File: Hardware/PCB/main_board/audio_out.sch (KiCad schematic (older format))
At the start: 2 parts, among them J5 Conn_Coaxial, J6 AudioJack2

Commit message: Flip connectors, add 3D models
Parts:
- removed J6: AudioJack2, symbol Connector:AudioJack2
- added J6: AudioJack3, lib:audio_jack_3.5mm_KYCON_STX-3000, symbol Connector:AudioJack3
- J5: footprint (none) -> lib:rca_black
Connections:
- wire segments 3 -> 4
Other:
- note added: "mono -> ring unused"
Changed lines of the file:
@@
 F 0 "J5" H 7650 1775 50  0000 L CNN
 F 1 "Conn_Coaxial" H 7650 1684 50  0000 L CNN
-F 2 "" H 7550 1800 50  0001 C CNN
+F 2 "lib:rca_black" H 7550 1800 50  0001 C CNN
 F 3 " ~" H 7550 1800 50  0001 C CNN
 	1    7550 1800
@@
 Wire Wire Line
 	7550 2050 7550 2000
-$Comp
-L Connector:AudioJack2 J6
-U 1 1 5E685921
-P 7550 3100
-F 0 "J6" H 7370 3083 50  0000 R CNN
-F 1 "AudioJack2" H 7370 3174 50  0000 R CNN
-F 2 "" H 7550 3100 50  0001 C CNN
-F 3 "~" H 7550 3100 50  0001 C CNN
-	1    7550 3100
-	-1   0    0    1
-$EndComp
 $Comp
 L power:GND #PWR018
@@
 Text Notes 7750 3450 0    118  ~ 24
 Audio headphones level
+$Comp
+L Connector:AudioJack3 J6
+U 1 1 5E55D40F
+P 7550 3100
+F 0 "J6" H 7270 3033 50  0000 R CNN
+F 1 "AudioJack3" H 7270 3124 50  0000 R CNN
+F 2 "lib:audio_jack_3.5mm_KYCON_STX-3000" H 7550 3100 50  0001 C CNN
+F 3 "~" H 7550 3100 50  0001 C CNN
+	1    7550 3100
+	-1   0    0    1
+$EndComp
+Wire Wire Line
+	7350 3000 6950 3000
+Text Notes 7350 3100 2    50   ~ 0
+mono -> ring unused
 $EndSCHEMATC

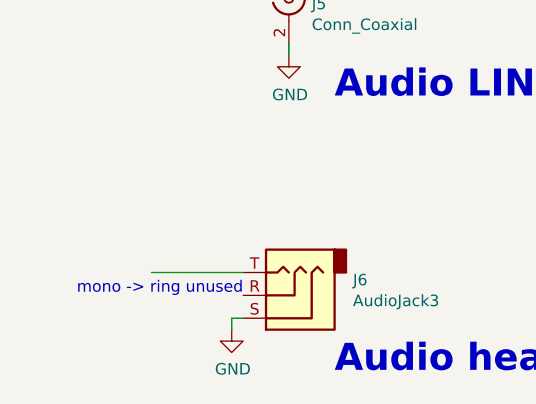
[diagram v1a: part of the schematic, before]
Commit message: Route GPIO
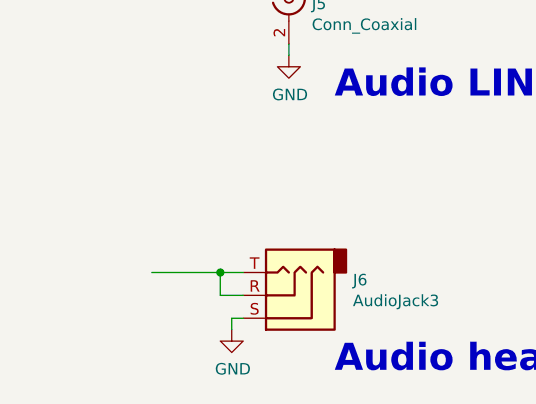
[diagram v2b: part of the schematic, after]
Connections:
- wire segments 4 -> 7
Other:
- note removed: "mono -> ring unused"
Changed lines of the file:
@@
 $Descr A4 11693 8268
 encoding utf-8
-Sheet 5 7
+Sheet 4 7
 Title ""
 Date ""
@@
 $EndComp
 Wire Wire Line
-	7350 3000 6950 3000
-Text Notes 7350 3100 2    50   ~ 0
-mono -> ring unused
+	7350 3000 7250 3000
+Wire Wire Line
+	7350 3100 7250 3100
+Wire Wire Line
+	7250 3100 7250 3000
+Connection ~ 7250 3000
+Wire Wire Line
+	7250 3000 6950 3000
 $EndSCHEMATC

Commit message: Route PWR
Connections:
- no-connect marks 0 -> 2
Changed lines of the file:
@@
 Wire Wire Line
 	7250 3000 6950 3000
+NoConn ~ 7350 1800
+NoConn ~ 6950 3000
 $EndSCHEMATC

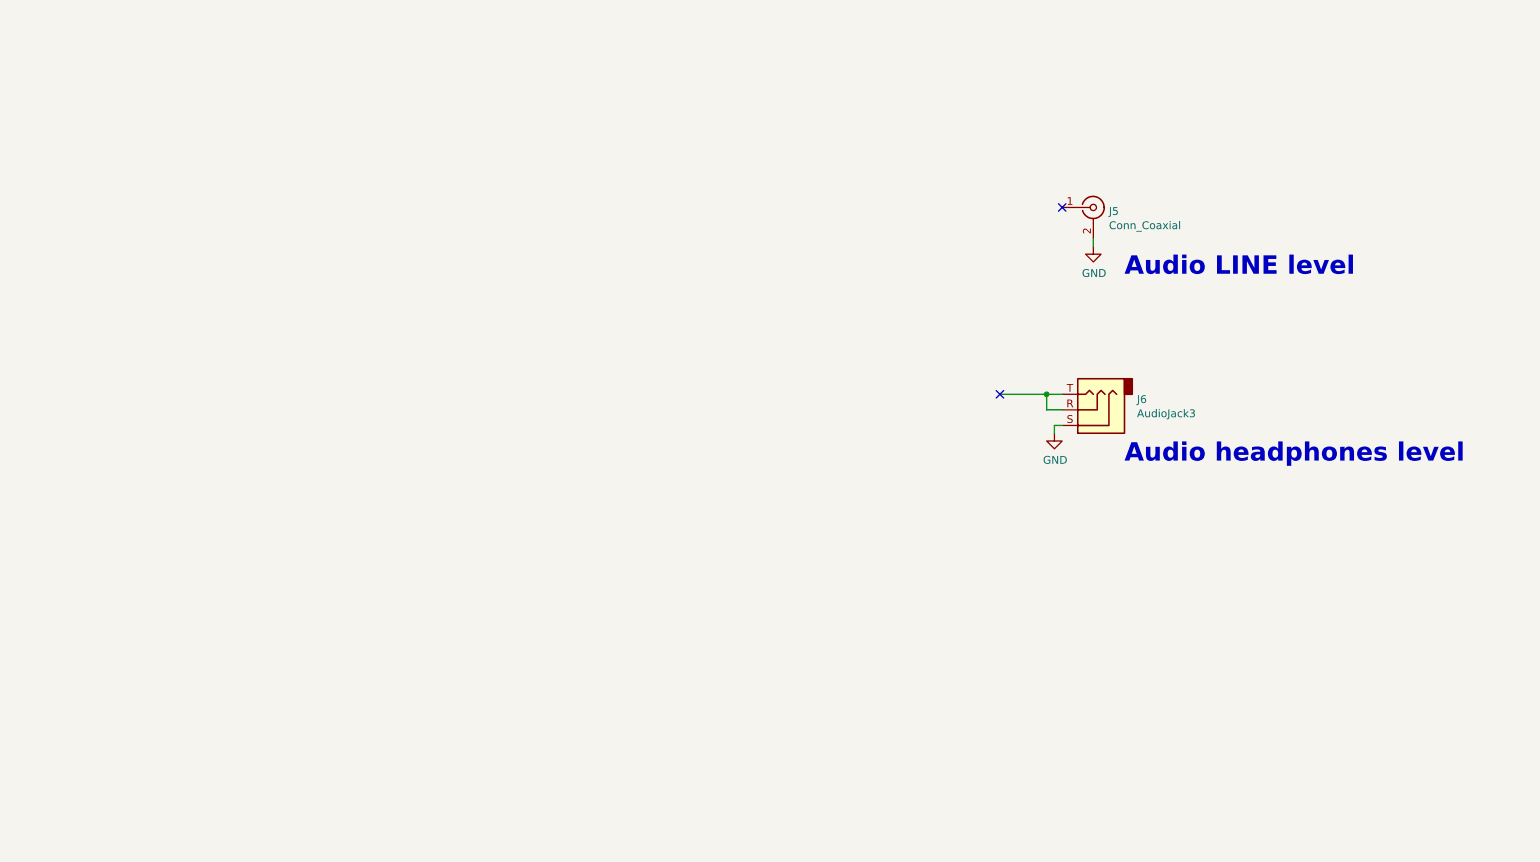
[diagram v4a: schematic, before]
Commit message: Add FX buffer and headphone amp to schematics
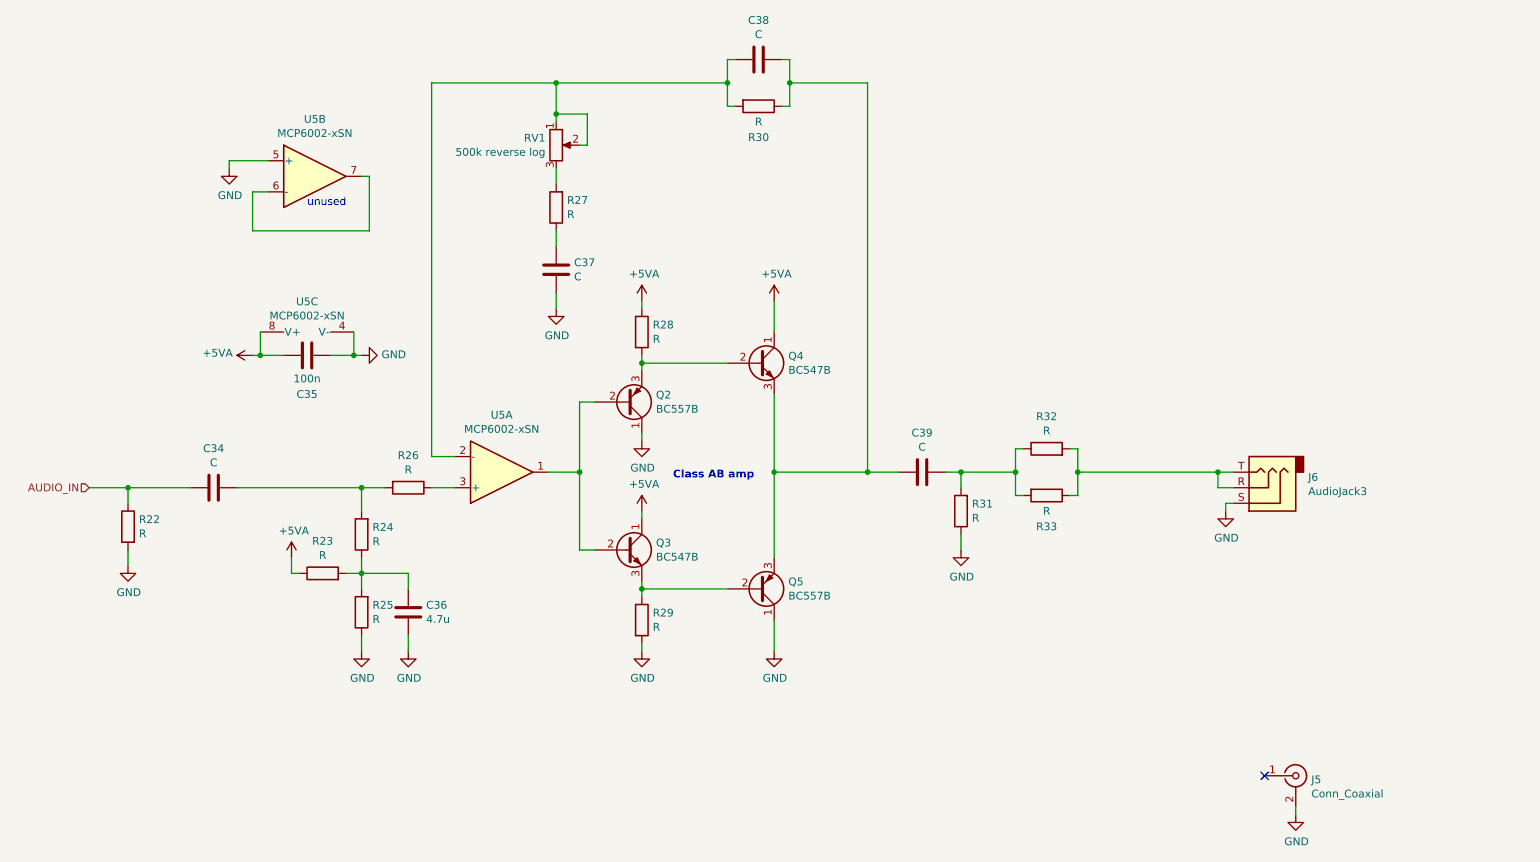
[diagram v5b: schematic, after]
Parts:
- added C34, C37, C38, C39: C, symbol Device:C
- added C35: 100n, symbol Device:C
- added C36: 4.7u, symbol Device:C
- added Q2, Q5: BC557B, Package_TO_SOT_THT:TO-92_Inline, symbol Transistor_BJT:BC557
- added Q3, Q4: BC547B, Package_TO_SOT_THT:TO-92_Inline, symbol Transistor_BJT:BC547
- added R22, R23, R24, R25, R26, R27, R28, R29, R30, R31, R32, R33: R, symbol Device:R
- added RV1: 500k reverse log, symbol Device:R_POT
- added U5: MCP6002-xSN, symbol Amplifier_Operational:MCP6002-xSN
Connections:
- net GND: now also C35.1, C36.1, C37.1, Q2.1 (C), Q5.1 (C), R22.2, R25.1, R29.2, R31.1, U5.4 (V-), U5.5 (+)
- net at J6.R, J6.T: now also R32.2, R33.1
- new net: R26.1, U5.3 (+)
- new net: C34.1, R24.2, R26.2
- new net: Q2.2 (B), Q3.2 (B), U5.1
- new net: C38.2, R30.2, RV1.1, RV1.2, U5.2 (-)
- new net: U5.6 (-), U5.7
- new net: R27.2, RV1.3
- new net: Q2.3 (E), Q4.2 (B), R28.2
- new net: C38.1, C39.2, Q4.3 (E), Q5.3 (E), R30.1
- new net: Q3.3 (E), Q5.2 (B), R29.1
- new net: C36.2, R23.2, R24.1, R25.2
- new net: C39.1, R31.2, R32.1, R33.2
- new net: C37.2, R27.1
- new net +5VA: C35.2, Q3.1 (C), Q4.1 (C), R23.1, R28.1, U5.8 (V+)
- new net AUDIO_IN: C34.2, R22.1
- no-connect marks 2 -> 1
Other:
- note added: "Class AB amp"
- note added: "unused"
- note removed: "Audio LINE level"
- note removed: "Audio headphones level"
- moved on the sheet: J5, J6

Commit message: Route PCB changes
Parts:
- removed C36: 4.7u, symbol Device:C
- removed C39: C, symbol Device:C
- removed Q2, Q5: BC557B, Package_TO_SOT_THT:TO-92_Inline, symbol Transistor_BJT:BC557
- removed Q3, Q4: BC547B, Package_TO_SOT_THT:TO-92_Inline, symbol Transistor_BJT:BC547
- added C36, C39: 47u, Capacitor_SMD:CP_Elec_6.3x5.4, symbol Device:CP
- added Q1, Q4: BC857B, Package_TO_SOT_SMD:SOT-23, symbol Transistor_BJT:BC857
- added Q2, Q3: BC847B, Package_TO_SOT_SMD:SOT-23, symbol Transistor_BJT:BC847
- C34: value C -> 100n; footprint (none) -> Capacitor_SMD:C_0805_2012Metric
- C35: footprint (none) -> Capacitor_SMD:C_0805_2012Metric
- C37: value C -> 4.7u; footprint (none) -> Capacitor_SMD:C_0805_2012Metric
- C38: value C -> 150p; footprint (none) -> Capacitor_SMD:C_0805_2012Metric
- R22: value R -> 22M; footprint (none) -> Resistor_SMD:R_0805_2012Metric
- R23, R25, R28, R29, R31: value R -> 10k; footprint (none) -> Resistor_SMD:R_0805_2012Metric
- R24: value R -> 10M; footprint (none) -> Resistor_SMD:R_0805_2012Metric
- R26: value R -> 1k; footprint (none) -> Resistor_SMD:R_0805_2012Metric
- R27: value R -> 33; footprint (none) -> Resistor_SMD:R_0805_2012Metric
- R30: value R -> 56k; footprint (none) -> Resistor_SMD:R_0805_2012Metric
- R32, R33: value R -> 100; footprint (none) -> Resistor_SMD:R_0805_2012Metric
- RV_VOL1: renamed from RV1; footprint (none) -> Potentiometer_THT:Potentiometer_Alps_RK09K_Single_Vertical
- U5: footprint (none) -> Package_SO:SOIC-8_3.9x4.9mm_P1.27mm
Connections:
- net +5VA: now also Q2.3 (C), Q3.3 (C)
- net GND: now also C36.2, Q1.3 (C), Q4.3 (C)
- net at U5.1: now also Q1.1 (B), Q2.1 (B)
- net at R28.2: now also Q1.2 (E), Q3.1 (B)
- net at C38.1, R30.1: now also C39.1, Q3.2 (E), Q4.2 (E)
- net at R29.1: now also Q2.2 (E), Q4.1 (B)
- net at R23.2, R24.1, R25.2: now also C36.1
- net at R31.2, R32.1, R33.2: now also C39.2

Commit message: Add test points headers
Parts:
- added J12: Audio_post_AB_amp, Connector_PinHeader_2.54mm:PinHeader_1x01_P2.54mm_Vertical, symbol Connector_Generic:Conn_01x01
- added J13: Audio_out_jack, Connector_PinHeader_2.54mm:PinHeader_1x01_P2.54mm_Vertical, symbol Connector_Generic:Conn_01x01
- added J14: Audio_out_RCA, Connector_PinHeader_2.54mm:PinHeader_1x01_P2.54mm_Vertical, symbol Connector_Generic:Conn_01x01
- added J9: Audio_pre_AB_amp, Connector_PinHeader_2.54mm:PinHeader_1x01_P2.54mm_Vertical, symbol Connector_Generic:Conn_01x01
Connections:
- net Audio_out_jack: now reaches J6.R, J6.T, R32.2, R33.1
- net Audio_out_jack: now also J13.1 (Pin_1)
- net Audio_out_RCA: now reaches J5.1 (In)
- net Audio_out_RCA: now also J14.1 (Pin_1)
- net audio_pre_AB_amp: now reaches Q1.1 (B), Q2.1 (B), U5.1
- net audio_pre_AB_amp: now also J9.1 (Pin_1)
- net audio_post_AB_amp: now reaches C38.1, C39.1, Q3.2 (E), Q4.2 (E), R30.1
- net audio_post_AB_amp: now also J12.1 (Pin_1)
- no-connect marks 1 -> 0
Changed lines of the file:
@@
 Wire Wire Line
 	7450 3500 7450 3650
-NoConn ~ 8650 5450
 Wire Wire Line
 	7450 3500 8350 3500
@@
 	1    0    0    1
 $EndComp
+Wire Wire Line
+	9200 1200 9100 1200
+Wire Wire Line
+	9100 1500 9200 1500
+Wire Wire Line
+	9100 1800 9200 1800
+Text Label 7650 3500 0    50   ~ 0
+Audio_out_jack
+Text Label 9100 1800 2    50   ~ 0
+Audio_out_jack
+Text Label 5550 3500 0    50   ~ 0
+audio_post_AB_amp
+Text Label 4250 3800 1    50   ~ 0
+audio_pre_AB_amp
+Text Label 9100 1500 2    50   ~ 0
+audio_post_AB_amp
+Text Label 9100 1200 2    50   ~ 0
+audio_pre_AB_amp
+Wire Wire Line
+	9100 2100 9200 2100
+Text Label 9100 2100 2    50   ~ 0
+Audio_out_RCA
+Text Label 8550 5450 2    50   ~ 0
+Audio_out_RCA
+Wire Wire Line
+	8550 5450 8650 5450
+$Comp
+L Connector_Generic:Conn_01x01 J?
+U 1 1 5E8E9A39
+P 9400 1200
+AR Path="/5E57C92D/5E8E9A39" Ref="J?"  Part="1"
+AR Path="/5E68385C/5E8E9A39" Ref="J9"  Part="1"
+F 0 "J9" H 9480 1242 50  0000 L CNN
+F 1 "Audio_pre_AB_amp" H 9480 1151 50  0000 L CNN
+F 2 "Connector_PinHeader_2.54mm:PinHeader_1x01_P2.54mm_Vertical" H 9400 1200 50  0001 C CNN
+F 3 "~" H 9400 1200 50  0001 C CNN
+	1    9400 1200
+	1    0    0    -1
+$EndComp
+$Comp
+L Connector_Generic:Conn_01x01 J?
+U 1 1 5E8EC39B
+P 9400 1500
+AR Path="/5E57C92D/5E8EC39B" Ref="J?"  Part="1"
+AR Path="/5E68385C/5E8EC39B" Ref="J12"  Part="1"
+F 0 "J12" H 9480 1542 50  0000 L CNN
+F 1 "Audio_post_AB_amp" H 9480 1451 50  0000 L CNN
+F 2 "Connector_PinHeader_2.54mm:PinHeader_1x01_P2.54mm_Vertical" H 9400 1500 50  0001 C CNN
+F 3 "~" H 9400 1500 50  0001 C CNN
+	1    9400 1500
+	1    0    0    -1
+$EndComp
+$Comp
+L Connector_Generic:Conn_01x01 J?
+U 1 1 5E8ECAF9
+P 9400 1800
+AR Path="/5E57C92D/5E8ECAF9" Ref="J?"  Part="1"
+AR Path="/5E68385C/5E8ECAF9" Ref="J13"  Part="1"
+F 0 "J13" H 9480 1842 50  0000 L CNN
+F 1 "Audio_out_jack" H 9480 1751 50  0000 L CNN
+F 2 "Connector_PinHeader_2.54mm:PinHeader_1x01_P2.54mm_Vertical" H 9400 1800 50  0001 C CNN
+F 3 "~" H 9400 1800 50  0001 C CNN
+	1    9400 1800
+	1    0    0    -1
+$EndComp
+$Comp
+L Connector_Generic:Conn_01x01 J?
+U 1 1 5E8EF8B9
+P 9400 2100
+AR Path="/5E57C92D/5E8EF8B9" Ref="J?"  Part="1"
+AR Path="/5E68385C/5E8EF8B9" Ref="J14"  Part="1"
+F 0 "J14" H 9480 2142 50  0000 L CNN
+F 1 "Audio_out_RCA" H 9480 2051 50  0000 L CNN
+F 2 "Connector_PinHeader_2.54mm:PinHeader_1x01_P2.54mm_Vertical" H 9400 2100 50  0001 C CNN
+F 3 "~" H 9400 2100 50  0001 C CNN
+	1    9400 2100
+	1    0    0    -1
+$EndComp
 $EndSCHEMATC

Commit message: Re-layout HMI, pre route
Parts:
- removed J14: Audio_out_RCA, Connector_PinHeader_2.54mm:PinHeader_1x01_P2.54mm_Vertical, symbol Connector_Generic:Conn_01x01
- removed J5: Conn_Coaxial, lib:rca_black, symbol Connector:Conn_Coaxial
- J12: value Audio_post_AB_amp -> Post_AB_amp; footprint Connector_PinHeader_2.54mm:PinHeader_1x01_P2.54mm_Vertical -> TestPoint:TestPoint_THTPad_D1.0mm_Drill0.5mm; symbol Connector_Generic:Conn_01x01 -> Connector:TestPoint
- J13: footprint Connector_PinHeader_2.54mm:PinHeader_1x01_P2.54mm_Vertical -> TestPoint:TestPoint_THTPad_D1.0mm_Drill0.5mm; symbol Connector_Generic:Conn_01x01 -> Connector:TestPoint
- J9: value Audio_pre_AB_amp -> Pre_AB_amp; footprint Connector_PinHeader_2.54mm:PinHeader_1x01_P2.54mm_Vertical -> TestPoint:TestPoint_THTPad_D1.0mm_Drill0.5mm; symbol Connector_Generic:Conn_01x01 -> Connector:TestPoint
- RV_VOL1: footprint Potentiometer_THT:Potentiometer_Alps_RK09K_Single_Vertical -> Potentiometer_THT:Potentiometer_Alps_RK09K_Single_Horizontal
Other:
- note added: "Test points"
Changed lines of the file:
@@
 $EndDescr
-$Comp
-L Connector:Conn_Coaxial J5
-U 1 1 5E6845CE
-P 8850 5450
-F 0 "J5" H 8950 5425 50  0000 L CNN
-F 1 "Conn_Coaxial" H 8950 5334 50  0000 L CNN
-F 2 "lib:rca_black" H 8850 5450 50  0001 C CNN
-F 3 " ~" H 8850 5450 50  0001 C CNN
-	1    8850 5450
-	1    0    0    -1
-$EndComp
-$Comp
-L power:GND #PWR019
-U 1 1 5E684B9C
-P 8850 5700
-F 0 "#PWR019" H 8850 5450 50  0001 C CNN
-F 1 "GND" H 8855 5527 50  0000 C CNN
-F 2 "" H 8850 5700 50  0001 C CNN
-F 3 "" H 8850 5700 50  0001 C CNN
-	1    8850 5700
-	1    0    0    -1
-$EndComp
-Wire Wire Line
-	8850 5700 8850 5650
 $Comp
 L power:GND #PWR018
@@
 F 0 "RV_VOL1" H 4031 1446 50  0000 R CNN
 F 1 "500k reverse log" H 4031 1355 50  0000 R CNN
-F 2 "Potentiometer_THT:Potentiometer_Alps_RK09K_Single_Vertical" H 4100 1400 50  0001 C CNN
+F 2 "Potentiometer_THT:Potentiometer_Alps_RK09K_Single_Horizontal" H 4100 1400 50  0001 C CNN
 F 3 "~" H 4100 1400 50  0001 C CNN
 	1    4100 1400
@@
 Text Label 9100 1200 2    50   ~ 0
 audio_pre_AB_amp
-Wire Wire Line
-	9100 2100 9200 2100
-Text Label 9100 2100 2    50   ~ 0
-Audio_out_RCA
-Text Label 8550 5450 2    50   ~ 0
-Audio_out_RCA
-Wire Wire Line
-	8550 5450 8650 5450
-$Comp
-L Connector_Generic:Conn_01x01 J?
+$Comp
+L Connector:TestPoint J?
 U 1 1 5E8E9A39
-P 9400 1200
+P 9200 1200
 AR Path="/5E57C92D/5E8E9A39" Ref="J?"  Part="1"
 AR Path="/5E68385C/5E8E9A39" Ref="J9"  Part="1"
-F 0 "J9" H 9480 1242 50  0000 L CNN
-F 1 "Audio_pre_AB_amp" H 9480 1151 50  0000 L CNN
-F 2 "Connector_PinHeader_2.54mm:PinHeader_1x01_P2.54mm_Vertical" H 9400 1200 50  0001 C CNN
-F 3 "~" H 9400 1200 50  0001 C CNN
-	1    9400 1200
-	1    0    0    -1
-$EndComp
-$Comp
-L Connector_Generic:Conn_01x01 J?
+F 0 "J9" V 9280 1242 50  0000 L CNN
+F 1 "Pre_AB_amp" V 9200 1400 50  0000 L CNN
+F 2 "TestPoint:TestPoint_THTPad_D1.0mm_Drill0.5mm" H 9200 1200 50  0001 C CNN
+F 3 "~" H 9200 1200 50  0001 C CNN
+	1    9200 1200
+	0    1    1    0
+$EndComp
+$Comp
+L Connector:TestPoint J?
 U 1 1 5E8EC39B
-P 9400 1500
+P 9200 1500
 AR Path="/5E57C92D/5E8EC39B" Ref="J?"  Part="1"
 AR Path="/5E68385C/5E8EC39B" Ref="J12"  Part="1"
-F 0 "J12" H 9480 1542 50  0000 L CNN
-F 1 "Audio_post_AB_amp" H 9480 1451 50  0000 L CNN
-F 2 "Connector_PinHeader_2.54mm:PinHeader_1x01_P2.54mm_Vertical" H 9400 1500 50  0001 C CNN
-F 3 "~" H 9400 1500 50  0001 C CNN
-	1    9400 1500
-	1    0    0    -1
-$EndComp
-$Comp
-L Connector_Generic:Conn_01x01 J?
+F 0 "J12" V 9280 1542 50  0000 L CNN
+F 1 "Post_AB_amp" V 9200 1700 50  0000 L CNN
+F 2 "TestPoint:TestPoint_THTPad_D1.0mm_Drill0.5mm" H 9200 1500 50  0001 C CNN
+F 3 "~" H 9200 1500 50  0001 C CNN
+	1    9200 1500
+	0    1    1    0
+$EndComp
+Text Notes 9000 2100 0    118  ~ 0
+Test points
+$Comp
+L Connector:TestPoint J?
 U 1 1 5E8ECAF9
-P 9400 1800
+P 9200 1800
 AR Path="/5E57C92D/5E8ECAF9" Ref="J?"  Part="1"
 AR Path="/5E68385C/5E8ECAF9" Ref="J13"  Part="1"
-F 0 "J13" H 9480 1842 50  0000 L CNN
-F 1 "Audio_out_jack" H 9480 1751 50  0000 L CNN
-F 2 "Connector_PinHeader_2.54mm:PinHeader_1x01_P2.54mm_Vertical" H 9400 1800 50  0001 C CNN
-F 3 "~" H 9400 1800 50  0001 C CNN
-	1    9400 1800
-	1    0    0    -1
-$EndComp
-$Comp
-L Connector_Generic:Conn_01x01 J?
-U 1 1 5E8EF8B9
-P 9400 2100
-AR Path="/5E57C92D/5E8EF8B9" Ref="J?"  Part="1"
-AR Path="/5E68385C/5E8EF8B9" Ref="J14"  Part="1"
-F 0 "J14" H 9480 2142 50  0000 L CNN
-F 1 "Audio_out_RCA" H 9480 2051 50  0000 L CNN
-F 2 "Connector_PinHeader_2.54mm:PinHeader_1x01_P2.54mm_Vertical" H 9400 2100 50  0001 C CNN
-F 3 "~" H 9400 2100 50  0001 C CNN
-	1    9400 2100
-	1    0    0    -1
+F 0 "J13" V 9280 1842 50  0000 L CNN
+F 1 "Audio_out_jack" V 9200 2000 50  0000 L CNN
+F 2 "TestPoint:TestPoint_THTPad_D1.0mm_Drill0.5mm" H 9200 1800 50  0001 C CNN
+F 3 "~" H 9200 1800 50  0001 C CNN
+	1    9200 1800
+	0    1    1    0
 $EndComp
 $EndSCHEMATC
